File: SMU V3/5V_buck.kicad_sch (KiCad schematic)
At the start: 15 parts, among them U5 ETQ-P3M150KVN, U6 TPS5430DDAR

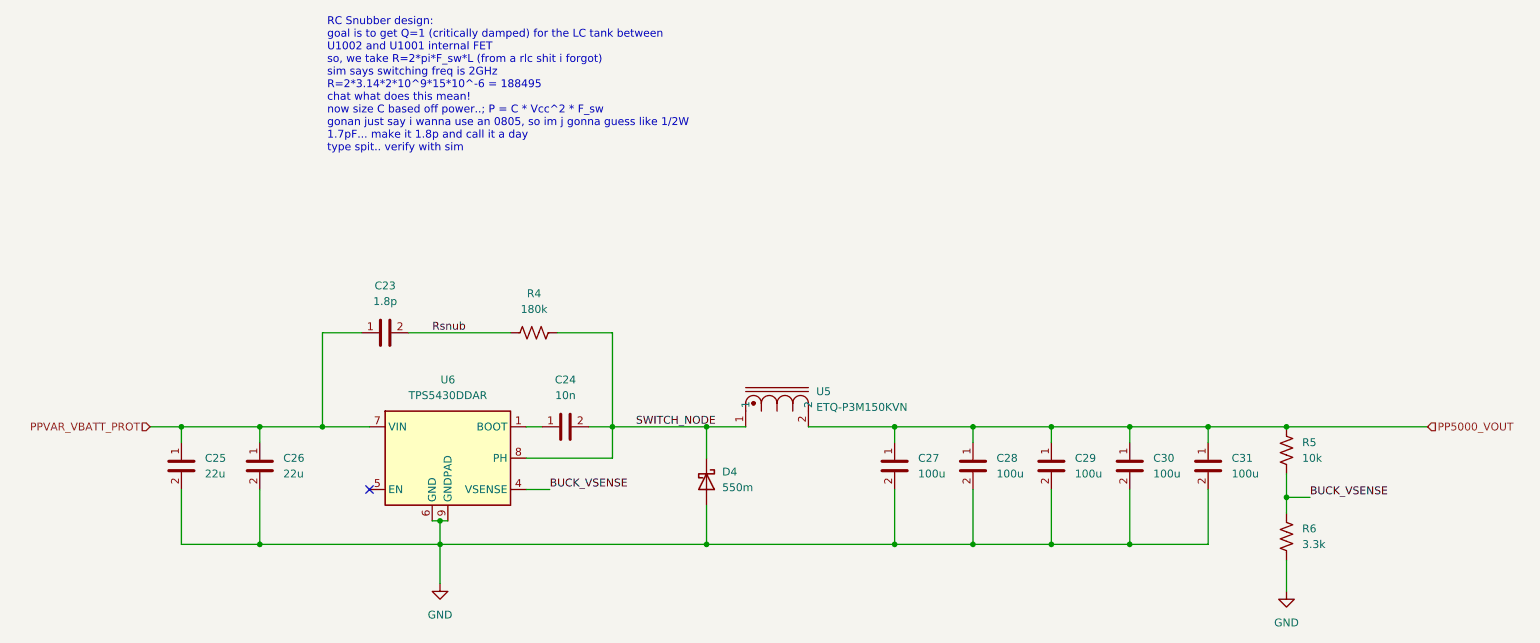
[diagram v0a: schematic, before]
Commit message: improved V3
added uart/spi test points and status leds
removed main 3v3 ldo
added silkscreen
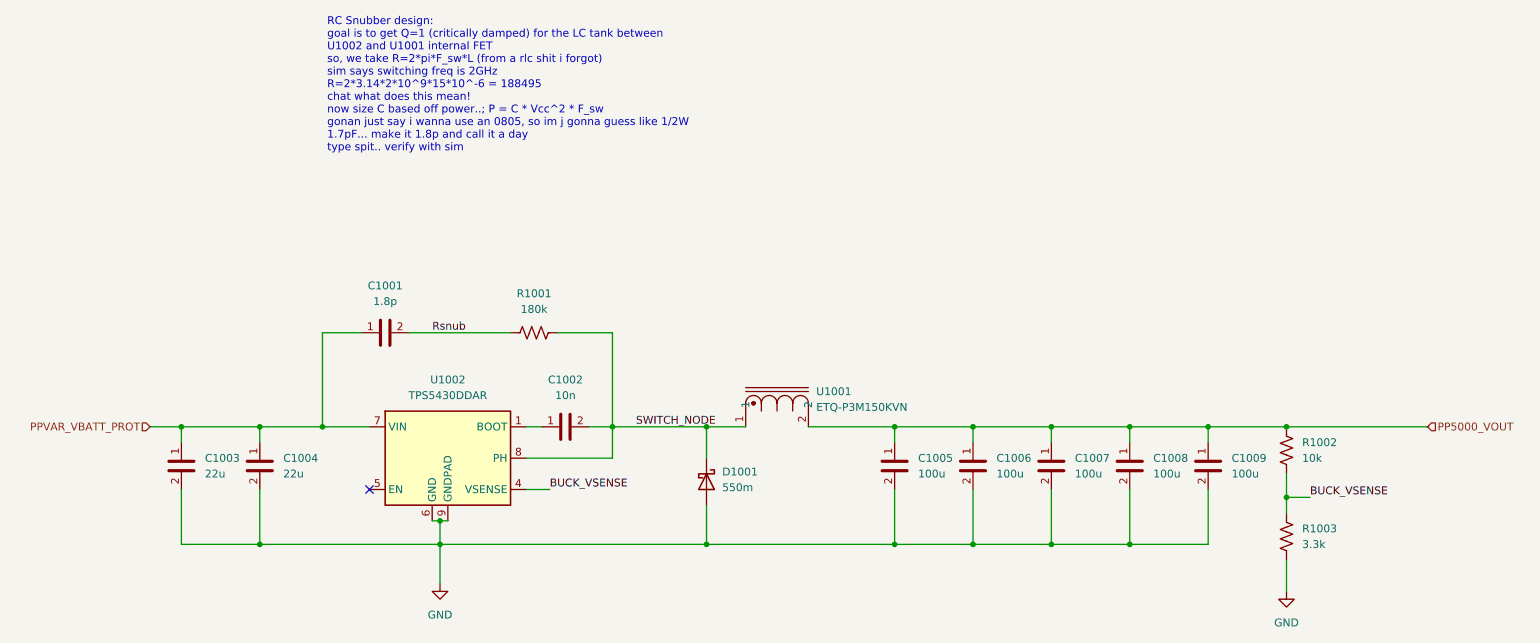
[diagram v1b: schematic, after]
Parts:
- renumbered C23 to C1001, C24 to C1002, C25 to C1003, C26 to C1004, C27 to C1005, C28 to C1006, C29 to C1007, C30 to C1008, C31 to C1009, D4 to D1001, R4 to R1001, R5 to R1002, R6 to R1003, U5 to U1001, U6 to U1002
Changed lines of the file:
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@@
 		(dnp no)
 		(fields_autoplaced yes)
-		(property "Reference" "U5"
+		(property "Reference" "U1001"
 			(at 153.67 76.8349 90)
 			(show_name no)
@@
 			(project "SMU V3"
 				(path "/1f58b889-96e6-4877-90a3-5a655db5910b/b9f10619-4e5b-45af-b866-c6815d605ed5/af802241-6422-4666-a084-41c36db8cc4c"
-					(reference "U5")
+					(reference "U1001")
 					(unit 1)
 				)
@@
 		(dnp no)
 		(fields_autoplaced yes)
-		(property "Reference" "C24"
+		(property "Reference" "C1002"
 			(at 113.03 74.93 90)
 			(show_name no)
@@
 			(project "SMU V3"
 				(path "/1f58b889-96e6-4877-90a3-5a655db5910b/b9f10619-4e5b-45af-b866-c6815d605ed5/af802241-6422-4666-a084-41c36db8cc4c"
-					(reference "C24")
+					(reference "C1002")
 					(unit 1)
 				)
@@
 		(dnp no)
 		(fields_autoplaced yes)
-		(property "Reference" "#PWR026"
+		(property "Reference" "#PWR01002"
 			(at 229.87 115.57 0)
 			(hide yes)
@@
 			(project "SMU V3"
 				(path "/1f58b889-96e6-4877-90a3-5a655db5910b/b9f10619-4e5b-45af-b866-c6815d605ed5/af802241-6422-4666-a084-41c36db8cc4c"
-					(reference "#PWR026")
+					(reference "#PWR01002")
 					(unit 1)
 				)
@@
 		(dnp no)
 		(fields_autoplaced yes)
-		(property "Reference" "C23"
+		(property "Reference" "C1001"
 			(at 83.82 59.69 90)
 			(show_name no)
@@
 			(project "SMU V3"
 				(path "/1f58b889-96e6-4877-90a3-5a655db5910b/b9f10619-4e5b-45af-b866-c6815d605ed5/af802241-6422-4666-a084-41c36db8cc4c"
-					(reference "C23")
+					(reference "C1001")
 					(unit 1)
 				)
@@
 		(dnp no)
 		(fields_autoplaced yes)
-		(property "Reference" "C31"
+		(property "Reference" "C1009"
 			(at 220.98 87.6299 0)
 			(show_name no)
@@
 			(project "SMU V3"
 				(path "/1f58b889-96e6-4877-90a3-5a655db5910b/b9f10619-4e5b-45af-b866-c6815d605ed5/af802241-6422-4666-a084-41c36db8cc4c"
-					(reference "C31")
+					(reference "C1009")
 					(unit 1)
 				)
@@
 		(dnp no)
 		(fields_autoplaced yes)
-		(property "Reference" "D4"
+		(property "Reference" "D1001"
 			(at 138.43 89.8524 90)
 			(show_name no)
@@
 			(project "SMU V3"
 				(path "/1f58b889-96e6-4877-90a3-5a655db5910b/b9f10619-4e5b-45af-b866-c6815d605ed5/af802241-6422-4666-a084-41c36db8cc4c"
-					(reference "D4")
+					(reference "D1001")
 					(unit 1)
 				)
@@
 		(dnp no)
 		(fields_autoplaced yes)
-		(property "Reference" "R5"
+		(property "Reference" "R1002"
 			(at 232.41 85.0899 90)
 			(show_name no)
@@
 			(project "SMU V3"
 				(path "/1f58b889-96e6-4877-90a3-5a655db5910b/b9f10619-4e5b-45af-b866-c6815d605ed5/af802241-6422-4666-a084-41c36db8cc4c"
-					(reference "R5")
+					(reference "R1002")
 					(unit 1)
 				)
@@
 		(dnp no)
 		(fields_autoplaced yes)
-		(property "Reference" "U6"
+		(property "Reference" "U1002"
 			(at 93.98 74.93 0)
 			(show_name no)
@@
 			(project "SMU V3"
 				(path "/1f58b889-96e6-4877-90a3-5a655db5910b/b9f10619-4e5b-45af-b866-c6815d605ed5/af802241-6422-4666-a084-41c36db8cc4c"
-					(reference "U6")
+					(reference "U1002")
 					(unit 1)
 				)
@@
 		(dnp no)
 		(fields_autoplaced yes)
-		(property "Reference" "C28"
+		(property "Reference" "C1006"
 			(at 182.88 87.6299 0)
 			(show_name no)
@@
 			(project "SMU V3"
 				(path "/1f58b889-96e6-4877-90a3-5a655db5910b/b9f10619-4e5b-45af-b866-c6815d605ed5/af802241-6422-4666-a084-41c36db8cc4c"
-					(reference "C28")
+					(reference "C1006")
 					(unit 1)
 				)
@@
 		(dnp no)
 		(fields_autoplaced yes)
-		(property "Reference" "C25"
+		(property "Reference" "C1003"
 			(at 54.61 87.6299 0)
 			(show_name no)
@@
 			(project "SMU V3"
 				(path "/1f58b889-96e6-4877-90a3-5a655db5910b/b9f10619-4e5b-45af-b866-c6815d605ed5/af802241-6422-4666-a084-41c36db8cc4c"
-					(reference "C25")
+					(reference "C1003")
 					(unit 1)
 				)
@@
 		(dnp no)
 		(fields_autoplaced yes)
-		(property "Reference" "R6"
+		(property "Reference" "R1003"
 			(at 232.41 99.0599 90)
 			(show_name no)
@@
 			(project "SMU V3"
 				(path "/1f58b889-96e6-4877-90a3-5a655db5910b/b9f10619-4e5b-45af-b866-c6815d605ed5/af802241-6422-4666-a084-41c36db8cc4c"
-					(reference "R6")
+					(reference "R1003")
 					(unit 1)
 				)
@@
 		(dnp no)
 		(fields_autoplaced yes)
-		(property "Reference" "C26"
+		(property "Reference" "C1004"
 			(at 67.31 87.6299 0)
 			(show_name no)
@@
 			(project "SMU V3"
 				(path "/1f58b889-96e6-4877-90a3-5a655db5910b/b9f10619-4e5b-45af-b866-c6815d605ed5/af802241-6422-4666-a084-41c36db8cc4c"
-					(reference "C26")
+					(reference "C1004")
 					(unit 1)
 				)
@@
 		(dnp no)
 		(fields_autoplaced yes)
-		(property "Reference" "C29"
+		(property "Reference" "C1007"
 			(at 195.58 87.6299 0)
 			(show_name no)
@@
 			(project "SMU V3"
 				(path "/1f58b889-96e6-4877-90a3-5a655db5910b/b9f10619-4e5b-45af-b866-c6815d605ed5/af802241-6422-4666-a084-41c36db8cc4c"
-					(reference "C29")
+					(reference "C1007")
 					(unit 1)
 				)
@@
 		(dnp no)
 		(fields_autoplaced yes)
-		(property "Reference" "C27"
+		(property "Reference" "C1005"
 			(at 170.18 87.6299 0)
 			(show_name no)
@@
 			(project "SMU V3"
 				(path "/1f58b889-96e6-4877-90a3-5a655db5910b/b9f10619-4e5b-45af-b866-c6815d605ed5/af802241-6422-4666-a084-41c36db8cc4c"
-					(reference "C27")
+					(reference "C1005")
 					(unit 1)
 				)
@@
 		(dnp no)
 		(fields_autoplaced yes)
-		(property "Reference" "#PWR025"
+		(property "Reference" "#PWR01001"
 			(at 92.71 114.3 0)
 			(hide yes)
@@
 			(project "SMU V3"
 				(path "/1f58b889-96e6-4877-90a3-5a655db5910b/b9f10619-4e5b-45af-b866-c6815d605ed5/af802241-6422-4666-a084-41c36db8cc4c"
-					(reference "#PWR025")
+					(reference "#PWR01001")
 					(unit 1)
 				)
@@
 		(dnp no)
 		(fields_autoplaced yes)
-		(property "Reference" "R4"
+		(property "Reference" "R1001"
 			(at 107.95 60.96 0)
 			(show_name no)
@@
 			(project "SMU V3"
 				(path "/1f58b889-96e6-4877-90a3-5a655db5910b/b9f10619-4e5b-45af-b866-c6815d605ed5/af802241-6422-4666-a084-41c36db8cc4c"
-					(reference "R4")
+					(reference "R1001")
 					(unit 1)
 				)
@@
 		(dnp no)
 		(fields_autoplaced yes)
-		(property "Reference" "C30"
+		(property "Reference" "C1008"
 			(at 208.28 87.6299 0)
 			(show_name no)
@@
 			(project "SMU V3"
 				(path "/1f58b889-96e6-4877-90a3-5a655db5910b/b9f10619-4e5b-45af-b866-c6815d605ed5/af802241-6422-4666-a084-41c36db8cc4c"
-					(reference "C30")
+					(reference "C1008")
 					(unit 1)
 				)
